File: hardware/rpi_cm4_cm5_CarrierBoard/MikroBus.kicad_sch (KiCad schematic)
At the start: 12 parts, among them J11 MIKROE-4247

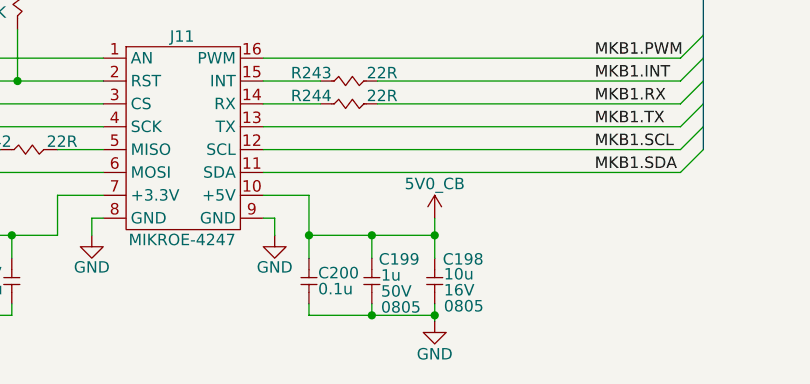
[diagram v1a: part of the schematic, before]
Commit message: Update preliminary placement, update DNP, regen BOM + Preliminary schematics
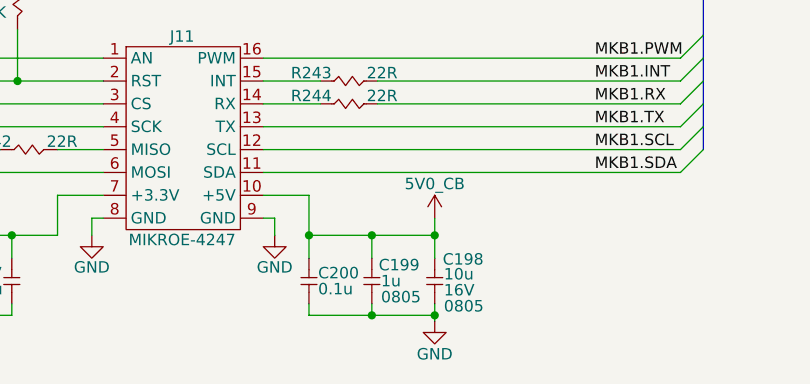
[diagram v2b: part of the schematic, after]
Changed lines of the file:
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@@
 		(dnp no)
 		(property "Reference" "C199"
-			(at 172.212 108.077 90)
+			(at 172.212 108.712 90)
 			(effects
 				(font
@@
 		)
 		(property "Value" "1u"
-			(at 172.466 109.855 90)
+			(at 172.466 110.49 90)
 			(effects
 				(font
@@
 		)
 		(property "Package" "0805"
-			(at 172.466 113.411 90)
+			(at 172.466 112.268 90)
 			(effects
 				(font
@@
 				)
 				(justify right)
+				(hide yes)
 			)
 		)

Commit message: Update PCB design rules for outer layers differential pairs Update preliminary component placement Update schematics based on PCB placement & remove duplicata / unnecessary components Update design notes and power table
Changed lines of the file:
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@@
 		)
 	)
-	(hierarchical_label "MBK1{MKB}"
+	(hierarchical_label "MKB1{MKB}"
 		(shape bidirectional)
 		(at 234.95 63.5 0)
